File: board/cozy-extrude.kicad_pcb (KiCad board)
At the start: 2 copper layers, 43.2 x 69.9 mm, 11 parts, among them J1 RPi-Pico-Socket, J2 BME280, J3 PWM-Fan, J4 Heater-Switch, K1 HF46F_5-HS1, U1 ULN2003

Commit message: improved pcb
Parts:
- removed Mount (x4): MountingHole_3.2mm_M3, MountingHole:MountingHole_3.2mm_M3
- added REF**: MountingHole_3.2mm_M3_Pad, MountingHole:MountingHole_3.2mm_M3_Pad, F.Cu at (4.55, 64.1)
- added REF**: MountingHole_3.2mm_M3_Pad, MountingHole:MountingHole_3.2mm_M3_Pad, F.Cu at (4.55, 4.40)
- added REF**: MountingHole_3.2mm_M3_Pad, MountingHole:MountingHole_3.2mm_M3_Pad, F.Cu at (38.8, 4.40)
- added REF**: MountingHole_3.2mm_M3_Pad, MountingHole:MountingHole_3.2mm_M3_Pad, F.Cu at (38.8, 64.1)
- J2: value BME280 -> BME280 Conn
- J3: value PWM-Fan -> PWM Fan Conn
- R1: value TACH-Pullup -> 2.2k
- moved J3 141.5 mm to (4.53, 31.1), turned to -90 degrees
- moved J2 126.5 mm to (33.8, 59.0)
- moved K1 126.0 mm to (33.8, 41.2)
- moved J4 125.9 mm to (36.3, 17.1)
- moved J1 125.4 mm to (10.9, 10.7)
- moved R1 124.6 mm to (18.5, 57.7)
- moved U1 108.5 mm to (23.6, 36.1), turned to 180 degrees
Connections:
- J1 pad 38: unconnected-(J1-Pad38) -> GND
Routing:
- net GND: track 93.6 -> 143.2 mm
- net /HEATER_EN: track 48.1 -> 6.17 mm
- net VBUS: track 73.7 -> 51.2 mm, vias 2 -> 0
- net +3V3: track 74.8 -> 93.7 mm
- net /TACH: track 21.7 -> 37.2 mm
- net Net-(K1-Pad1): track 51.5 -> 64.8 mm
- net /PWM: track 35.7 -> 24.5 mm
- net /CSB: track 10.0 -> 7.97 mm
- net /SDO: track 9.49 -> 8.13 mm
- net /SCL: track 7.46 -> 6.13 mm
- net /SDA: track 7.46 -> 6.13 mm
- net Net-(K1-Pad3): track 23.7 -> 22.5 mm
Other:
- board size 43.2 x 69.9 mm -> 41.9 x 67.3 mm

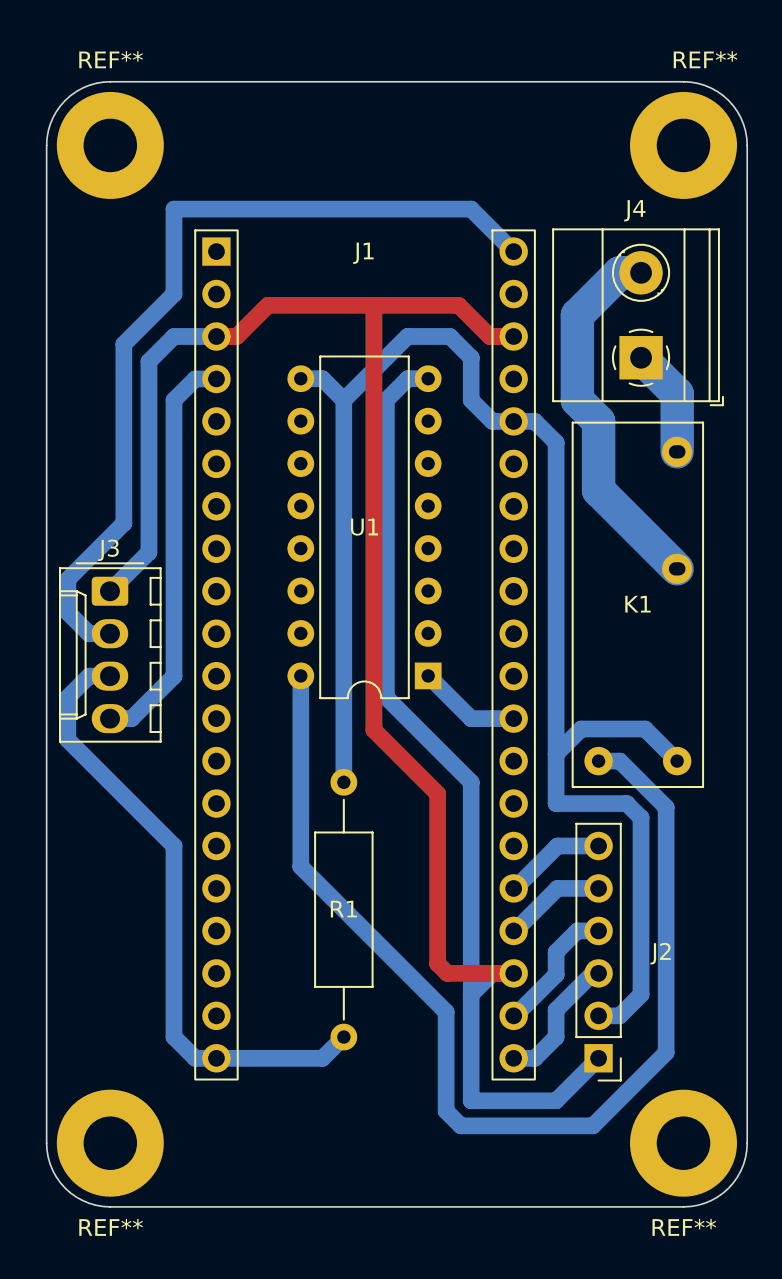
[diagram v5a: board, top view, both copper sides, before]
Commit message: adds swd port to pico-socket, some image exports for docs
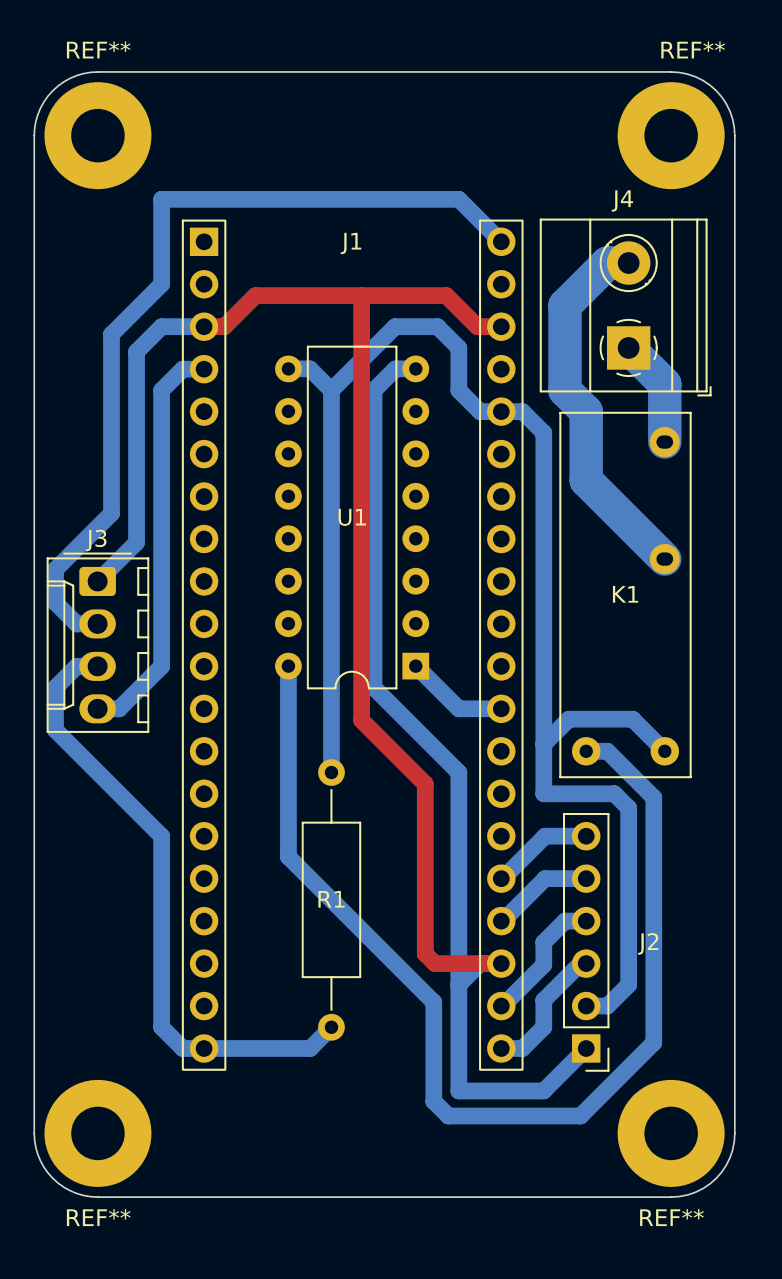
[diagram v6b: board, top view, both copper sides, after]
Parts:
- moved U1 0.94 mm to (22.8, 35.5)
- moved REF** 0.94 mm to (38.1, 3.81)
- moved J3 0.94 mm to (3.79, 30.5)
- moved J1 0.94 mm to (10.2, 10.2)
- moved REF** 0.94 mm to (3.81, 3.81)
- moved R1 0.94 mm to (17.8, 57.1)
- moved REF** 0.94 mm to (38.1, 63.5)
- moved J2 0.94 mm to (33.0, 58.4)
- moved J4 0.94 mm to (35.6, 16.5)
- moved K1 0.94 mm to (33.0, 40.6)
- moved REF** 0.94 mm to (3.81, 63.5)
